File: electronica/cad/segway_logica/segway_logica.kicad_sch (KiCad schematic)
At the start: 12 parts, among them J20 Cable lógica-potencia 2x8, J4 Paro MPT0,5 1=GND 2=PARO (NC), J7 Encoder IZQ PT1,5 1=GND 2=A 3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, J8 Encoder DER PT1,5 1=GND 2=A 3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

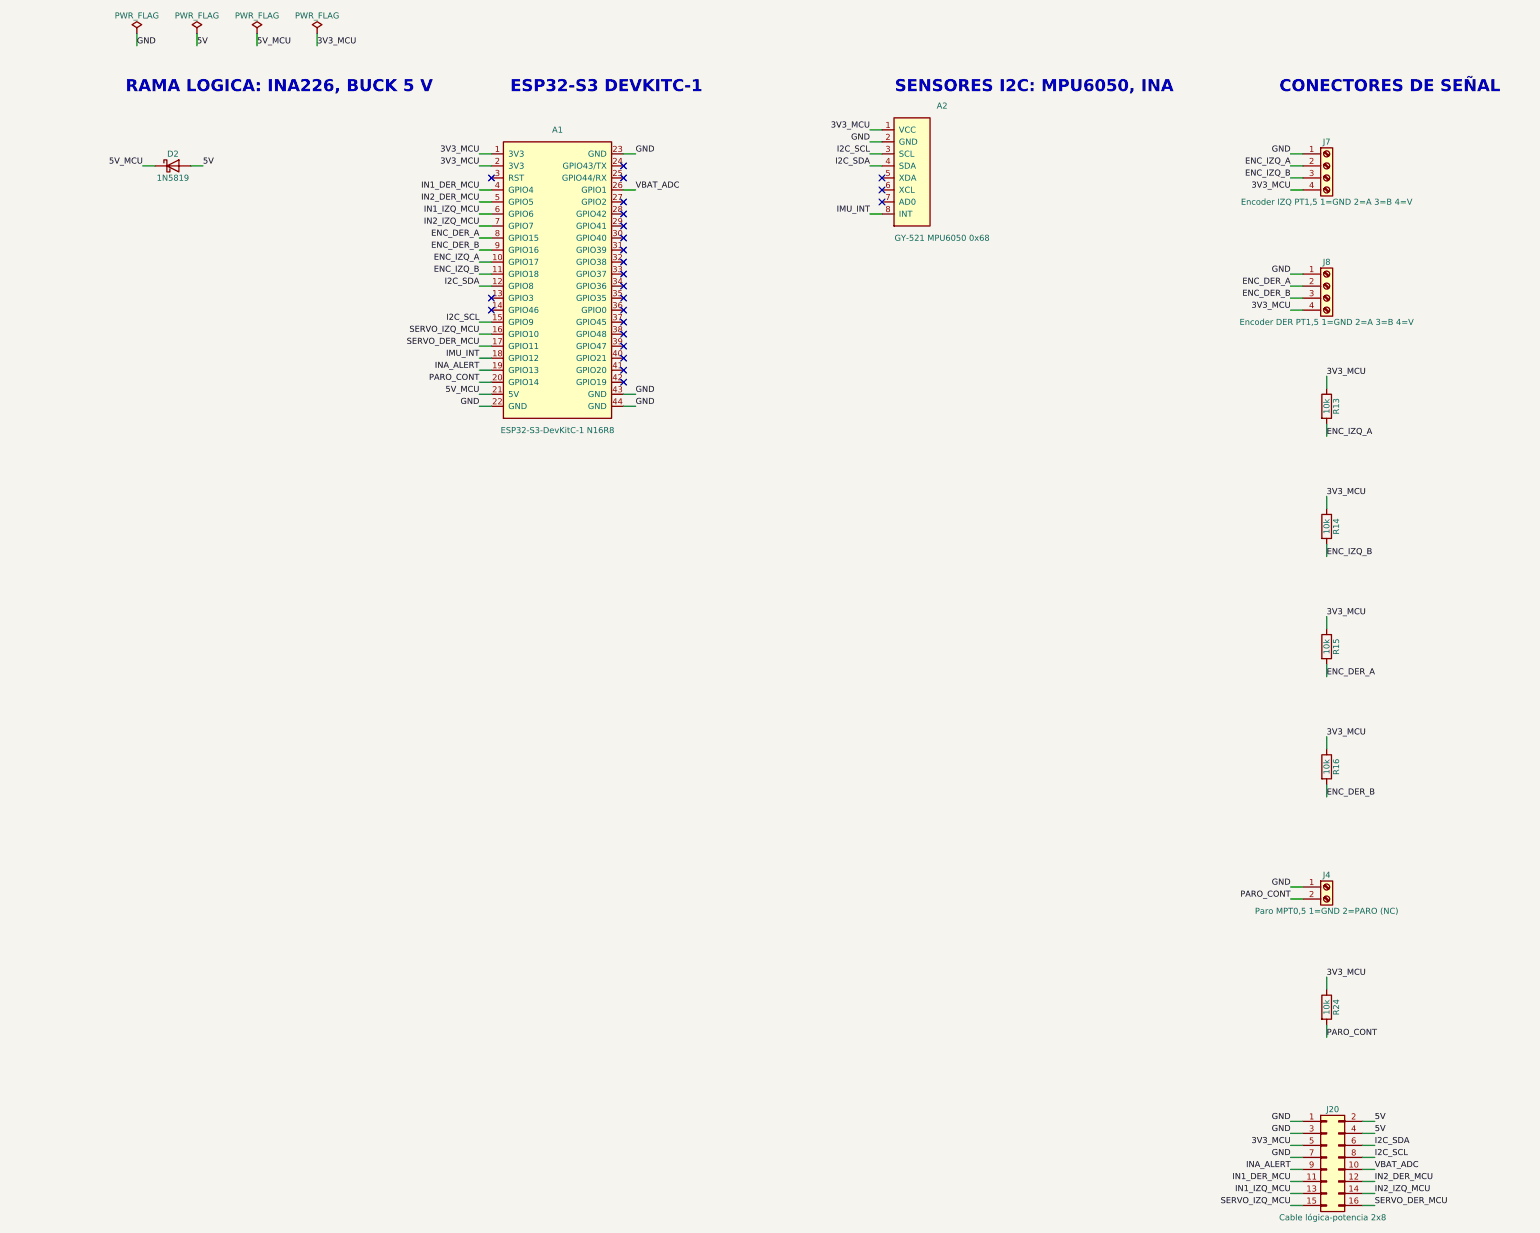
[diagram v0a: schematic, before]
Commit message: electronica: PCB v0.1 de la placa de lógica, una cara, DRC limpio (ELE-032)
- Ruteo a mano por topología (agente/placas/logica.py, TEC-04): DRC 0 errores,
  0 sin conectar, 0 de paridad; 2 puentes de alambre (3V3 17,8 mm y GND 7,6 mm).
- Mapa de GPIO y cable J20 elegidos por geometría: columna par del IDC en línea
  con A1.15-22; SCL/SDA pasan por el MPU. D2 pasa a la placa de potencia (5V_MCU
  por el cable); J7 con extremos invertidos. Esquemas de lógica y potencia
  regenerados: ERC 0 y netlist coincidente.
- construir_pcb.py con --placa y --fabricar: puentes fijos, áreas sin relleno,
  rótulos y escala en cobre, relleno con reglas reales, PDF 1:1, taladros.
- Supuestos SUP-04/15/24/26/28 cambiados y SUP-72 a SUP-74 nuevos.

Co-Authored-By: Claude Opus 5.5 <noreply@anthropic.com>
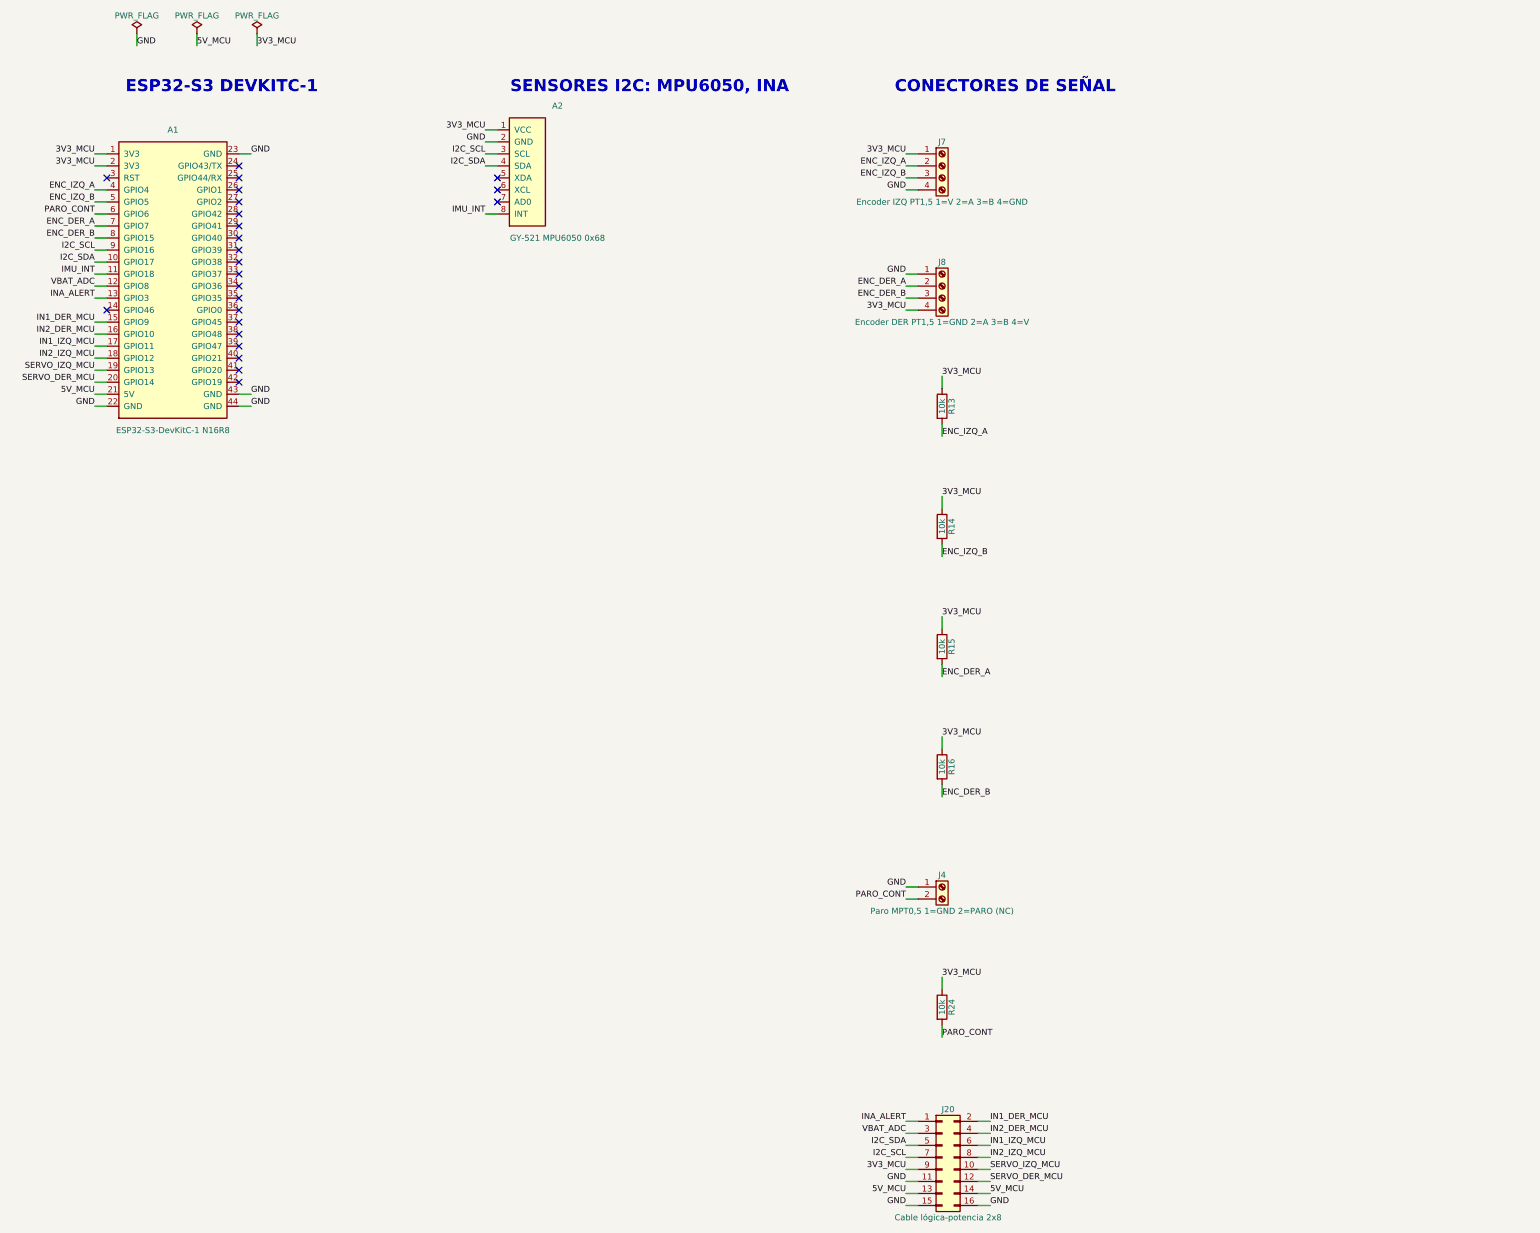
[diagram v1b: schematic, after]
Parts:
- removed D2: 1N5819, Diode_THT:D_DO-41_SOD81_P10.16mm_Horizontal, symbol Diode:1N5819
- J7: value Encoder IZQ PT1,5 1=GND 2=A 3=B 4=V -> Encoder IZQ PT1,5 1=V 2=A 3=B 4=GND; Estado provisorio [H] (reemplaza al XH-4: los hilos del encoder se atornillan; A/B por color [H], invertirlos solo cambia el signo; calibre sin medir: puntera de 0,25 mm² si es AWG 26-28; alternativa MPT 0,5 de 2,54 mm con el mismo orden) | v0.4: pin 4 en 3V3_PER (V_ENC unido, R30 eliminada, SUP-53, SUP-64); C20 eliminado (SUP-69) -> provisorio [H] (reemplaza al XH-4: los hilos del encoder se atornillan; A/B por color [H], invertirlos solo cambia el signo; calibre sin medir: puntera de 0,25 mm² si es AWG 26-28; alternativa MPT 0,5 de 2,54 mm con el mismo orden) | v0.4: pin 4 en 3V3_PER (V_ENC unido, R30 eliminada, SUP-53, SUP-64); C20 eliminado (SUP-69); pines 1 y 4 invertidos por ruteo (DEC-17)
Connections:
- net 3V3_MCU: now also J20.9 (Pin_9), J7.1 (Pin_1); no longer J20.5 (Pin_5), J7.4 (Pin_4)
- net 5V_MCU: now also J20.13 (Pin_13), J20.14 (Pin_14)
- net ENC_DER_A: now also A1.7 (GPIO7); no longer A1.8 (GPIO15)
- net ENC_DER_B: now also A1.8 (GPIO15); no longer A1.9 (GPIO16)
- net ENC_IZQ_A: now also A1.4 (GPIO4); no longer A1.10 (GPIO17)
- net ENC_IZQ_B: now also A1.5 (GPIO5); no longer A1.11 (GPIO18)
- net GND: now also J20.11 (Pin_11), J20.15 (Pin_15), J20.16 (Pin_16), J7.4 (Pin_4); no longer J20.1 (Pin_1), J20.3 (Pin_3), J20.7 (Pin_7), J7.1 (Pin_1)
- net I2C_SCL: now also A1.9 (GPIO16), J20.7 (Pin_7); no longer A1.15 (GPIO9), J20.8 (Pin_8)
- net I2C_SDA: now also A1.10 (GPIO17), J20.5 (Pin_5); no longer A1.12 (GPIO8), J20.6 (Pin_6)
- net IMU_INT: now also A1.11 (GPIO18); no longer A1.18 (GPIO12)
- net IN1_DER_MCU: now also A1.15 (GPIO9), J20.2 (Pin_2); no longer A1.4 (GPIO4), J20.11 (Pin_11)
- net IN1_IZQ_MCU: now also A1.17 (GPIO11), J20.6 (Pin_6); no longer A1.6 (GPIO6), J20.13 (Pin_13)
- net IN2_DER_MCU: now also A1.16 (GPIO10), J20.4 (Pin_4); no longer A1.5 (GPIO5), J20.12 (Pin_12)
- net IN2_IZQ_MCU: now also A1.18 (GPIO12), J20.8 (Pin_8); no longer A1.7 (GPIO7), J20.14 (Pin_14)
- net INA_ALERT: now also A1.13 (GPIO3), J20.1 (Pin_1); no longer A1.19 (GPIO13), J20.9 (Pin_9)
- net PARO_CONT: now also A1.6 (GPIO6); no longer A1.20 (GPIO14)
- net SERVO_DER_MCU: now also A1.20 (GPIO14), J20.12 (Pin_12); no longer A1.17 (GPIO11), J20.16 (Pin_16)
- net SERVO_IZQ_MCU: now also A1.19 (GPIO13), J20.10 (Pin_10); no longer A1.16 (GPIO10), J20.15 (Pin_15)
- net VBAT_ADC: now also A1.12 (GPIO8), J20.3 (Pin_3); no longer A1.26 (GPIO1), J20.10 (Pin_10)
- removed net 5V: J20.2 (Pin_2), J20.4 (Pin_4)
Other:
- note removed: "RAMA LOGICA: INA226, BUCK 5 V"

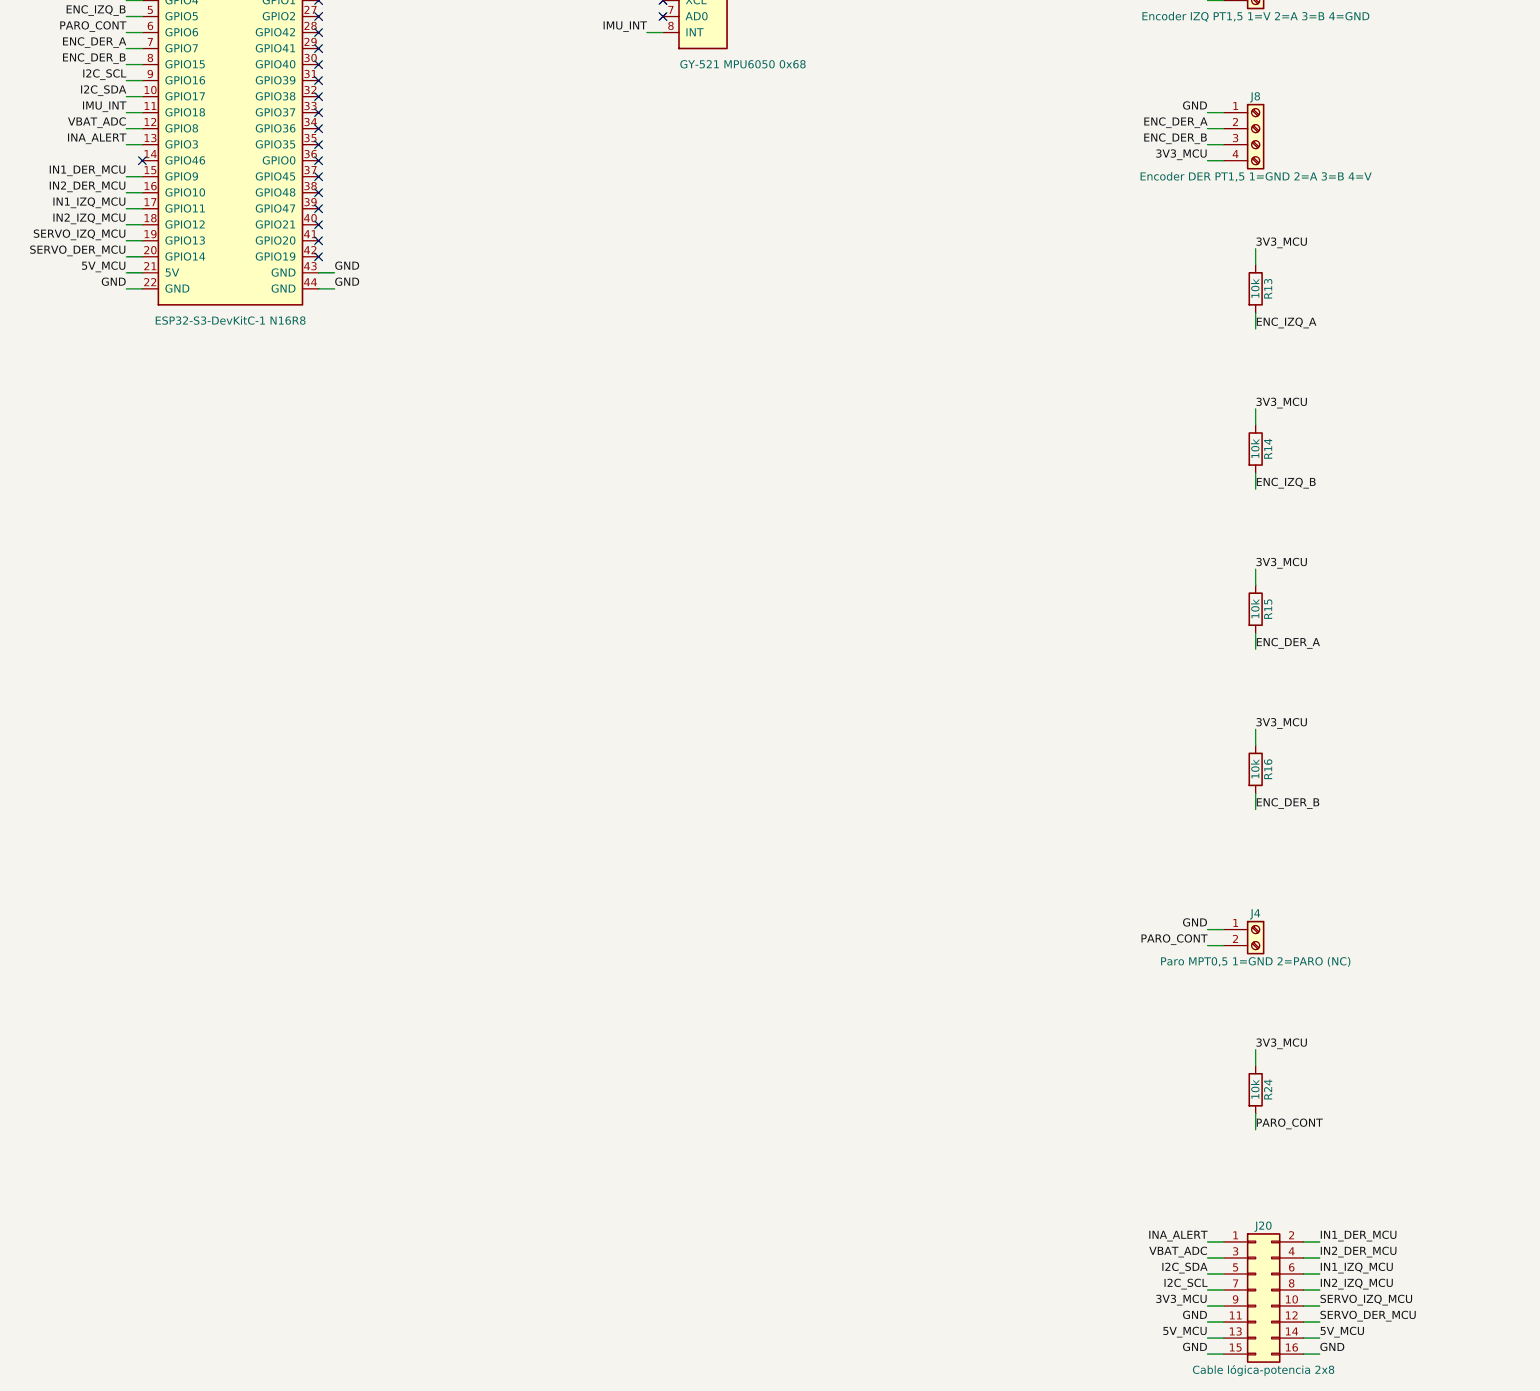
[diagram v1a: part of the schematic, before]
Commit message: electronica: PCB v0.1 de la placa de potencia, una cara, DRC limpio (ELE-032)
- Placa de potencia 150 x 110 mm: barra VM_BUS, lomo GND en estrella entre los
  pads de los fusibles, ramas por canal de motor, franja de servos y banda
  lógica. DRC 0 errores, 0 sin conectar, 0 de paridad; 7 puentes fijos.
- Ruteo híbrido (TEC-05): esqueleto y bus I2C a mano (J20 -> A7 -> A5 ->
  corredor bajo los módulos -> A6), Freerouting solo para nets simples, vías
  prohibidas sobre componentes y poda automática de puentes redundantes.
- Cable J20 y GPIO reordenados por geometría (VBAT en GPIO3, ALERT en GPIO8,
  columna par servos/IN); placa de lógica regenerada y re-verificada (0/0/0).
- J20.11 sin conexión en la potencia; INA226 sin separador opcional.
- Supuestos SUP-04/15/24/28/72 actualizados y SUP-75 a SUP-77 nuevos.

Co-Authored-By: Claude Opus 5.5 <noreply@anthropic.com>
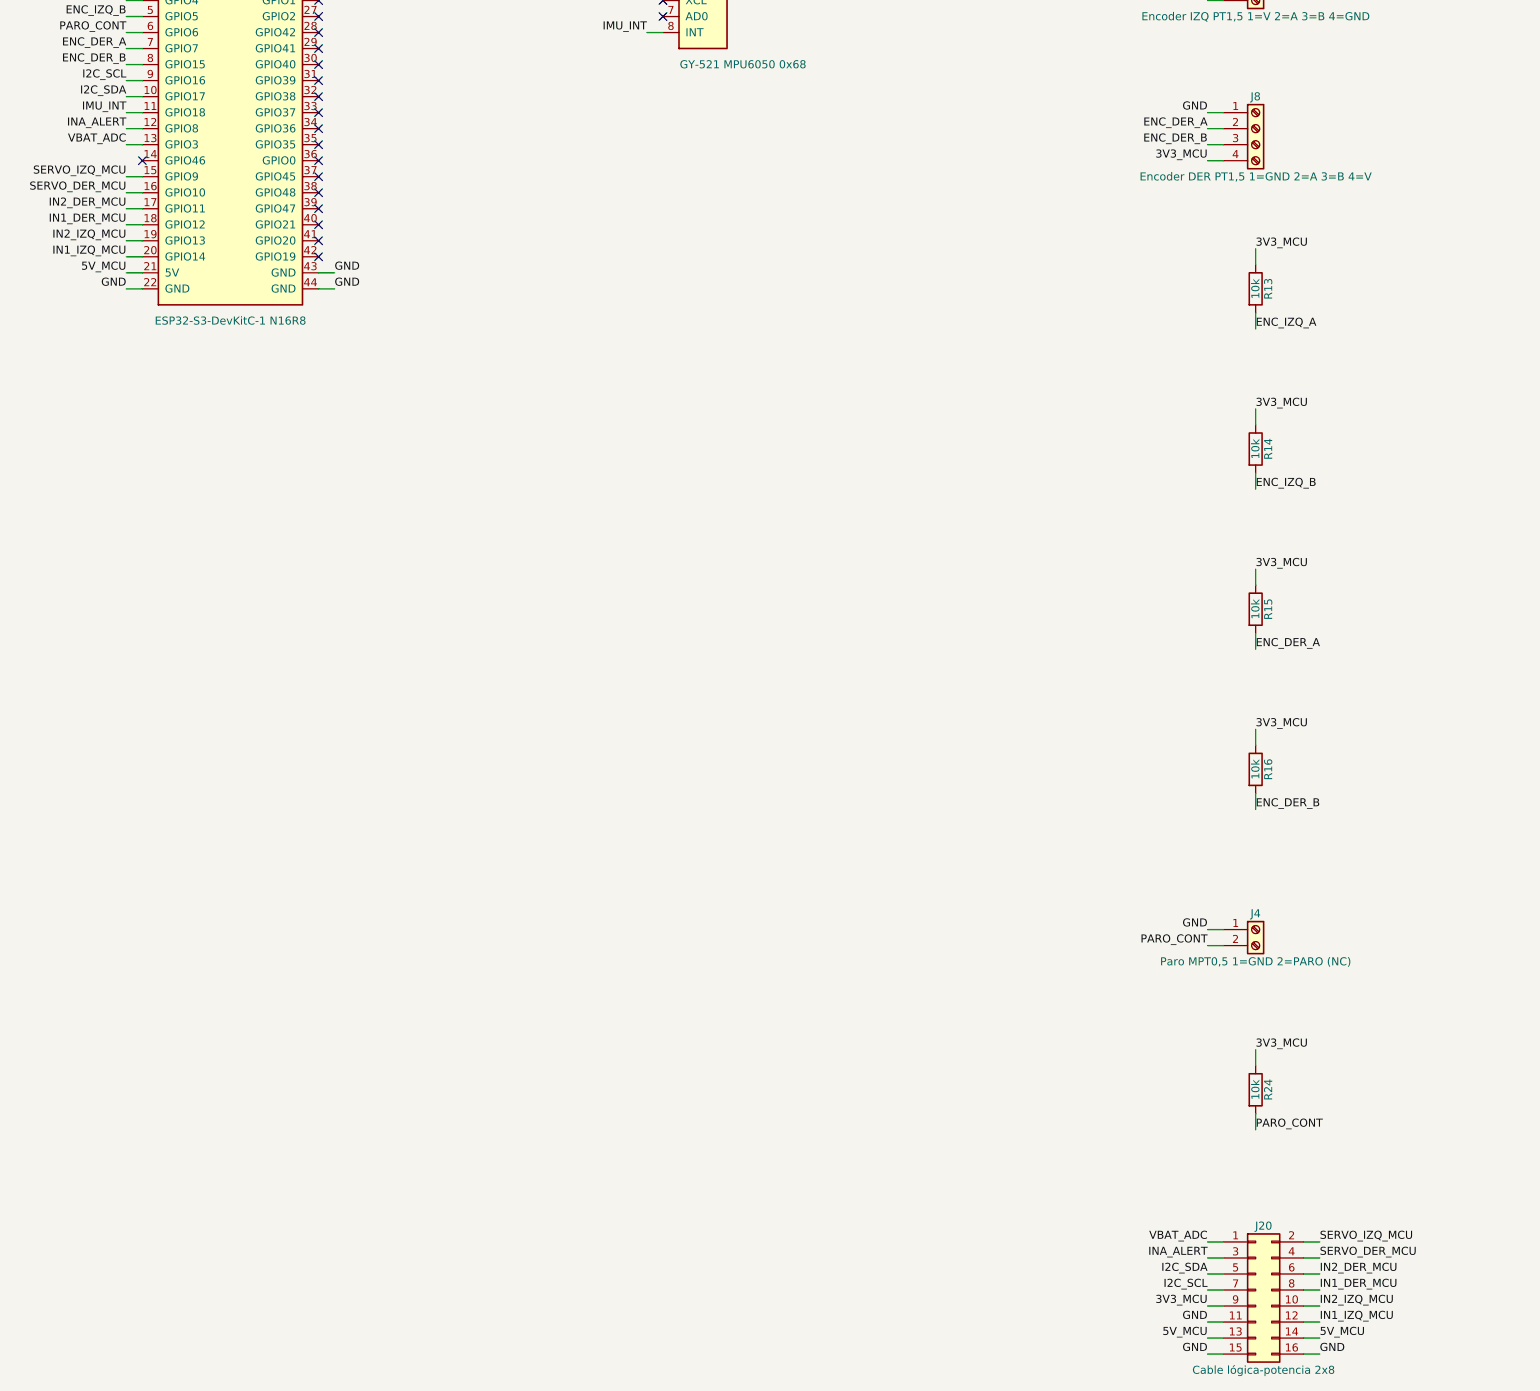
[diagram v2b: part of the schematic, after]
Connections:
- net IN1_DER_MCU: now also A1.18 (GPIO12), J20.8 (Pin_8); no longer A1.15 (GPIO9), J20.2 (Pin_2)
- net IN1_IZQ_MCU: now also A1.20 (GPIO14), J20.12 (Pin_12); no longer A1.17 (GPIO11), J20.6 (Pin_6)
- net IN2_DER_MCU: now also A1.17 (GPIO11), J20.6 (Pin_6); no longer A1.16 (GPIO10), J20.4 (Pin_4)
- net IN2_IZQ_MCU: now also A1.19 (GPIO13), J20.10 (Pin_10); no longer A1.18 (GPIO12), J20.8 (Pin_8)
- net INA_ALERT: now also A1.12 (GPIO8), J20.3 (Pin_3); no longer A1.13 (GPIO3), J20.1 (Pin_1)
- net SERVO_DER_MCU: now also A1.16 (GPIO10), J20.4 (Pin_4); no longer A1.20 (GPIO14), J20.12 (Pin_12)
- net SERVO_IZQ_MCU: now also A1.15 (GPIO9), J20.2 (Pin_2); no longer A1.19 (GPIO13), J20.10 (Pin_10)
- net VBAT_ADC: now also A1.13 (GPIO3), J20.1 (Pin_1); no longer A1.12 (GPIO8), J20.3 (Pin_3)
